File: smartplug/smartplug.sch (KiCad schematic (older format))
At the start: 17 parts, among them J1 Conn_01x03_Male, J2 Conn_01x03_Female, K1 ALA2F12, U1 RAC01-05SGA, U2 ADP2302ARDZ-5.0-R7, U3 PHOTON, U4 NUD3112LT1G

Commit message: added connector footprint and updated PCB
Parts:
- J1: footprint female_plug_new:TE_3-213598-2-new -> term_block_3pos:1985852
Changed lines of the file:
@@
 F 0 "J1" H 1256 2178 50  0000 C CNN
 F 1 "Conn_01x03_Male" H 1256 2087 50  0000 C CNN
-F 2 "female_plug_new:TE_3-213598-2-new" H 1150 1900 50  0001 C CNN
+F 2 "term_block_3pos:1985852" H 1150 1900 50  0001 C CNN
 F 3 "~" H 1150 1900 50  0001 C CNN
 	1    1150 1900

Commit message: Fixed clearances and added silkscreen
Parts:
- R1: footprint Resistor_SMD:R_0402_1005Metric -> Resistor_SMD:R_0805_2012Metric
- R2: value R -> 56
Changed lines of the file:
@@
 P 6500 3950
 F 0 "R2" H 6570 3996 50  0000 L CNN
-F 1 "R" H 6570 3905 50  0000 L CNN
+F 1 "56" H 6570 3905 50  0000 L CNN
 F 2 "Resistor_SMD:R_0805_2012Metric" V 6430 3950 50  0001 C CNN
 F 3 "~" H 6500 3950 50  0001 C CNN
@@
 F 0 "R1" H 1868 6396 50  0000 L CNN
 F 1 "100k" H 1868 6305 50  0000 L CNN
-F 2 "Resistor_SMD:R_0402_1005Metric" V 1840 6340 50  0001 C CNN
+F 2 "Resistor_SMD:R_0805_2012Metric" V 1840 6340 50  0001 C CNN
 F 3 "~" H 1800 6350 50  0001 C CNN
 	1    1800 6350

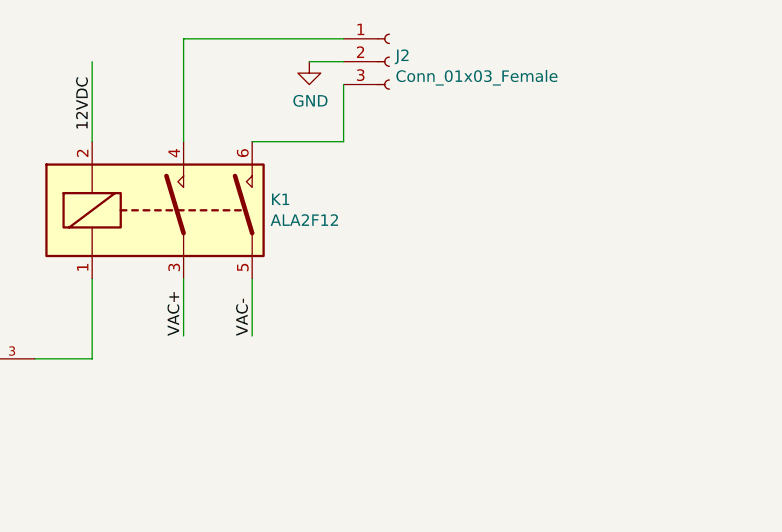
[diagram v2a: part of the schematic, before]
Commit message: rearranged board to reduce area
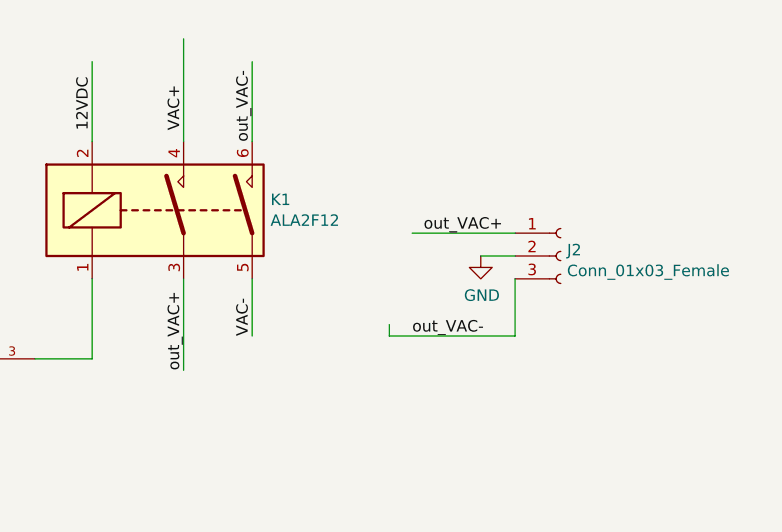
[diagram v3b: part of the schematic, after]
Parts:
- U3: footprint digikey-footprints:Particle_Photon -> particle:photon_smd
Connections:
- net labels added: out_VAC+, out_VAC-
- wire segments 43 -> 45
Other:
- moved on the sheet: J2
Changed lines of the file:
@@
 F 0 "U3" H 5250 3887 60  0000 C CNN
 F 1 "PHOTON" H 5250 3781 60  0000 C CNN
-F 2 "digikey-footprints:Particle_Photon" H 5250 3000 60  0001 C CNN
+F 2 "particle:photon_smd" H 5250 3000 60  0001 C CNN
 F 3 "" H 5250 3000 60  0000 C CNN
 	1    5250 2900
@@
 L Connector:Conn_01x03_Female J2
 U 1 1 5C93E3AE
-P 9900 1500
-F 0 "J2" H 9927 1526 50  0000 L CNN
-F 1 "Conn_01x03_Female" H 9927 1435 50  0000 L CNN
-F 2 "female_plug_new:TE_3-213598-2-new" H 9900 1500 50  0001 C CNN
-F 3 "~" H 9900 1500 50  0001 C CNN
-	1    9900 1500
+P 10650 2350
+F 0 "J2" H 10677 2376 50  0000 L CNN
+F 1 "Conn_01x03_Female" H 10677 2285 50  0000 L CNN
+F 2 "female_plug_new:TE_3-213598-2-new" H 10650 2350 50  0001 C CNN
+F 3 "~" H 10650 2350 50  0001 C CNN
+	1    10650 2350
 	1    0    0    -1
 $EndComp
@@
 L power:GND #PWR0105
 U 1 1 5C9426C3
-P 9550 1500
-F 0 "#PWR0105" H 9550 1250 50  0001 C CNN
-F 1 "GND" H 9555 1327 50  0000 C CNN
-F 2 "" H 9550 1500 50  0001 C CNN
-F 3 "" H 9550 1500 50  0001 C CNN
-	1    9550 1500
-	1    0    0    -1
-$EndComp
-Wire Wire Line
-	9700 1500 9550 1500
-Wire Wire Line
-	9700 1600 9700 1850
-Wire Wire Line
-	9700 1850 9300 1850
-Wire Wire Line
-	9700 1400 9000 1400
+P 10300 2350
+F 0 "#PWR0105" H 10300 2100 50  0001 C CNN
+F 1 "GND" H 10305 2177 50  0000 C CNN
+F 2 "" H 10300 2350 50  0001 C CNN
+F 3 "" H 10300 2350 50  0001 C CNN
+	1    10300 2350
+	1    0    0    -1
+$EndComp
+Wire Wire Line
+	10450 2350 10300 2350
+Wire Wire Line
+	10450 2450 10450 2700
 Wire Wire Line
 	9000 1400 9000 1850
 Wire Wire Line
-	9000 2450 9000 2700
-Wire Wire Line
 	9300 2450 9300 2700
-Text Label 9000 2700 1    50   ~ 0
-VAC+
 Text Label 9300 2700 1    50   ~ 0
 VAC-
@@
 	1    0    0    -1
 $EndComp
+Text Label 9000 1800 1    50   ~ 0
+VAC+
+Wire Wire Line
+	9300 1850 9300 1500
+Text Label 9300 1850 1    50   ~ 0
+out_VAC-
+Text Label 9000 2850 1    50   ~ 0
+out_VAC+
+Wire Wire Line
+	9000 2450 9000 2850
+Wire Wire Line
+	10450 2250 10000 2250
+Wire Wire Line
+	10450 2700 9900 2700
+Wire Wire Line
+	9900 2700 9900 2650
+Text Label 10050 2250 0    50   ~ 0
+out_VAC+
+Text Label 10000 2700 0    50   ~ 0
+out_VAC-
 $EndSCHEMATC
